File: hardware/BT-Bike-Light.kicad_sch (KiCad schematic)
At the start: 1 part, among them U1 BC805M

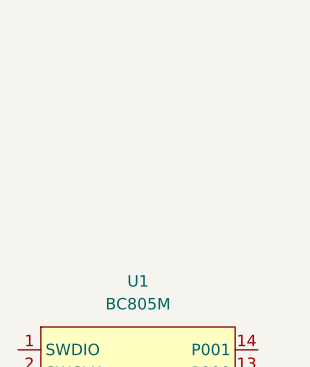
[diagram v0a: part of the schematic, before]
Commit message: Add XPE2 LED
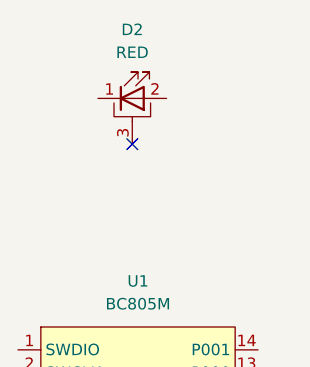
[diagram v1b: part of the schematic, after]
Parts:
- added D2: RED, LED_SMD:LED_Cree-XP, symbol Device:LED_Pad
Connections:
- no-connect marks 0 -> 1
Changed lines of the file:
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@@
 		(comment 1 "Ben Owen")
+	)
+	(no_connect
+		(at 139.7 69.85)
 	)
 	(wire
@@
 		)
 	)
+	(symbol
+		(lib_id "Device:LED_Pad")
+		(at 139.7 64.77 0)
+		(unit 1)
+		(exclude_from_sim no)
+		(in_bom yes)
+		(on_board yes)
+		(dnp no)
+		(fields_autoplaced yes)
+		(property "Reference" "D2"
+			(at 139.7 57.15 0)
+			(effects
+				(font
+					(size 1.27 1.27)
+				)
+			)
+		)
+		(property "Value" "RED"
+			(at 139.7 59.69 0)
+			(effects
+				(font
+					(size 1.27 1.27)
+				)
+			)
+		)
+		(property "Footprint" "LED_SMD:LED_Cree-XP"
+			(at 139.7 64.77 0)
+			(effects
+				(font
+					(size 1.27 1.27)
+				)
+				(hide yes)
+			)
+		)
+		(property "Datasheet" "~"
+			(at 139.7 64.77 0)
+			(effects
+				(font
+					(size 1.27 1.27)
+				)
+				(hide yes)
+			)
+		)
+		(property "Description" "Light emitting diode with pad"
+			(at 139.7 64.77 0)
+			(effects
+				(font
+					(size 1.27 1.27)
+				)
+				(hide yes)
+			)
+		)
+		(pin "2"
+		)
+		(pin "1"
+		)
+		(pin "3"
+		)
+		(instances
+			(project ""
+				(path "/3263b444-391f-435a-aeab-6f7fca8830e2"
+					(reference "D2")
+					(unit 1)
+				)
+			)
+		)
+	)

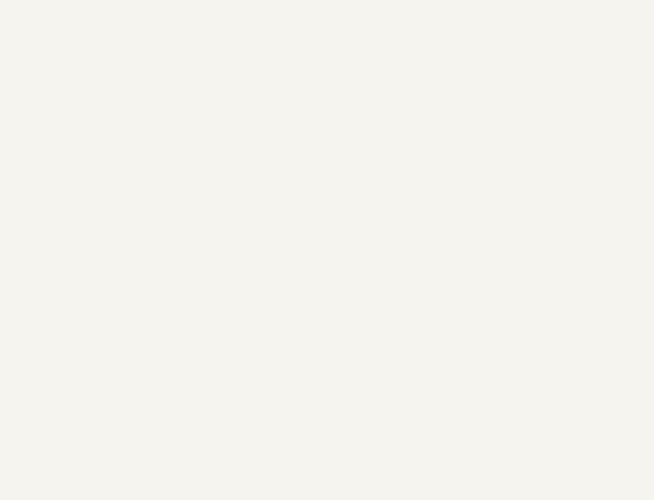
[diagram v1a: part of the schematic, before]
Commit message: Add debug connector
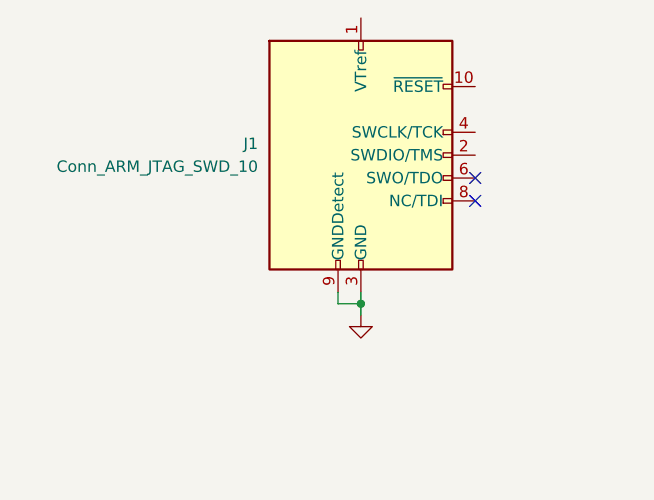
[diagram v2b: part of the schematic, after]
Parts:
- added J1: Conn_ARM_JTAG_SWD_10, Samtech:FTSH-107-01-F-DV-K, symbol Connector:Conn_ARM_JTAG_SWD_10
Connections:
- net GND: now also J1.3 (GND), J1.5 (GND), J1.9 (GNDDetect)
- no-connect marks 1 -> 3
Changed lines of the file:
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@@
 		(comment 1 "Ben Owen")
+	)
+	(junction
+		(at 72.39 63.5)
+		(diameter 0)
+		(color 0 0 0 0)
+	)
+	(no_connect
+		(at 85.09 49.53)
+	)
+	(no_connect
+		(at 85.09 52.07)
 	)
 	(no_connect
@@
 	(wire
 		(pts
+			(xy 72.39 63.5) (xy 72.39 64.77)
+		)
+		(stroke
+			(width 0)
+			(type default)
+		)
+	)
+	(wire
+		(pts
+			(xy 69.85 62.23) (xy 69.85 63.5)
+		)
+		(stroke
+			(width 0)
+			(type default)
+		)
+	)
+	(wire
+		(pts
 			(xy 156.21 110.49) (xy 156.21 107.95)
 		)
@@
 	(wire
 		(pts
+			(xy 72.39 62.23) (xy 72.39 63.5)
+		)
+		(stroke
+			(width 0)
+			(type default)
+		)
+	)
+	(wire
+		(pts
 			(xy 156.21 107.95) (xy 153.67 107.95)
+		)
+		(stroke
+			(width 0)
+			(type default)
+		)
+	)
+	(wire
+		(pts
+			(xy 69.85 63.5) (xy 72.39 63.5)
 		)
 		(stroke
@@
 					(unit 1)
 				)
+			)
+		)
+	)
+	(symbol
+		(lib_id "Connector:Conn_ARM_JTAG_SWD_10")
+		(at 72.39 46.99 0)
+		(unit 1)
+		(exclude_from_sim no)
+		(in_bom yes)
+		(on_board yes)
+		(dnp no)
+		(fields_autoplaced yes)
+		(property "Reference" "J1"
+			(at 60.96 45.7199 0)
+			(effects
+				(font
+					(size 1.27 1.27)
+				)
+				(justify right)
+			)
+		)
+		(property "Value" "Conn_ARM_JTAG_SWD_10"
+			(at 60.96 48.2599 0)
+			(effects
+				(font
+					(size 1.27 1.27)
+				)
+				(justify right)
+			)
+		)
+		(property "Footprint" "Samtech:FTSH-107-01-F-DV-K"
+			(at 72.39 46.99 0)
+			(effects
+				(font
+					(size 1.27 1.27)
+				)
+				(hide yes)
+			)
+		)
+		(property "Datasheet" "http://infocenter.arm.com/help/topic/com.arm.doc.ddi0314h/DDI0314H_coresight_components_trm.pdf"
+			(at 63.5 78.74 90)
+			(effects
+				(font
+					(size 1.27 1.27)
+				)
+				(hide yes)
+			)
+		)
+		(property "Description" "Cortex Debug Connector, standard ARM Cortex-M SWD and JTAG interface"
+			(at 72.39 46.99 0)
+			(effects
+				(font
+					(size 1.27 1.27)
+				)
+				(hide yes)
+			)
+		)
+		(pin "1"
+		)
+		(pin "7"
+		)
+		(pin "10"
+		)
+		(pin "4"
+		)
+		(pin "3"
+		)
+		(pin "8"
+		)
+		(pin "5"
+		)
+		(pin "9"
+		)
+		(pin "6"
+		)
+		(pin "2"
+		)
+		(instances
+			(project ""
+				(path "/3263b444-391f-435a-aeab-6f7fca8830e2"
+					(reference "J1")
+					(unit 1)
+				)
+			)
+		)
+	)
+	(symbol
+		(lib_id "power:GND")
+		(at 72.39 64.77 0)
+		(unit 1)
+		(exclude_from_sim no)
+		(in_bom yes)
+		(on_board yes)
+		(dnp no)
+		(fields_autoplaced yes)
+		(property "Reference" "#PWR02"
+			(at 72.39 71.12 0)
+			(effects
+				(font
+					(size 1.27 1.27)
+				)
+				(hide yes)
+			)
+		)
+		(property "Value" "GND"
+			(at 72.39 69.85 0)
+			(effects
+				(font
+					(size 1.27 1.27)
+				)
+				(hide yes)
+			)
+		)
+		(property "Footprint" ""
+			(at 72.39 64.77 0)
+			(effects
+				(font
+					(size 1.27 1.27)
+				)
+				(hide yes)
+			)
+		)
+		(property "Datasheet" ""
+			(at 72.39 64.77 0)
+			(effects
+				(font
+					(size 1.27 1.27)
+				)
+				(hide yes)
+			)
+		)
+		(property "Description" "Power symbol creates a global label with name \"GND\" , ground"
+			(at 72.39 64.77 0)
+			(effects
+				(font
+					(size 1.27 1.27)
+				)
+				(hide yes)
+			)
+		)
+		(pin "1"
+		)
+		(instances
+			(project "BT-Bike-Light"
+				(path "/3263b444-391f-435a-aeab-6f7fca8830e2"
+					(reference "#PWR02")
+					(unit 1)
+				)

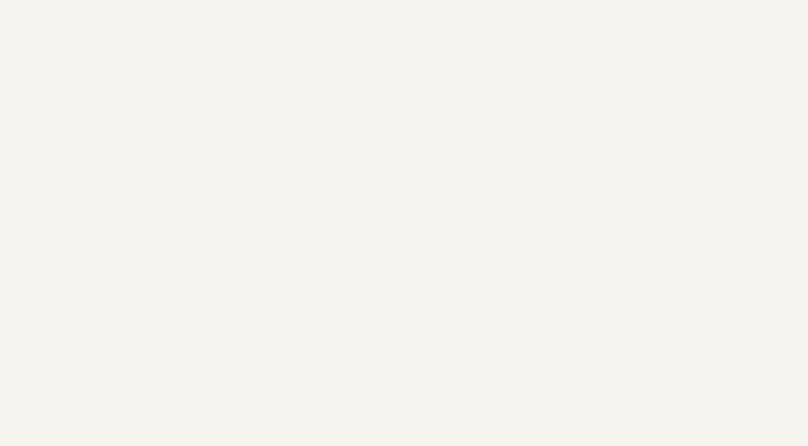
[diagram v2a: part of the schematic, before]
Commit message: Add accelerometer
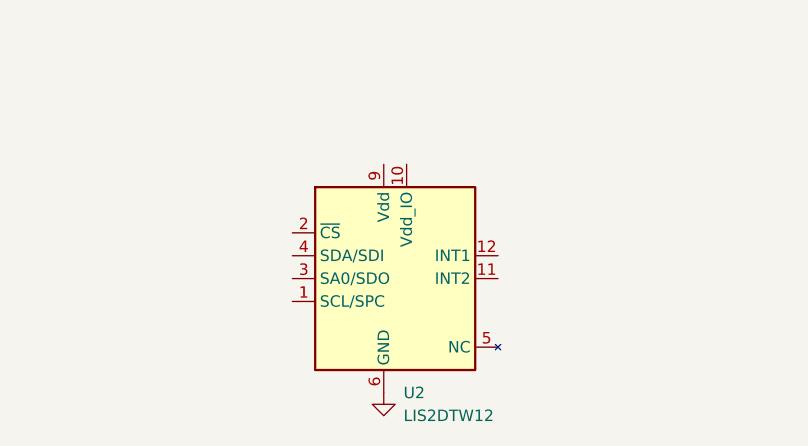
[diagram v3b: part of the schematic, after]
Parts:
- added U2: LIS2DTW12, Package_LGA:LGA-12_2x2mm_P0.5mm, symbol STMicroelectronics:LIS2DTW12
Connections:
- net GND: now also U2.6 (GND), U2.7 (GND), U2.8 (GND)
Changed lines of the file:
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@@
+	)
+	(symbol
+		(lib_id "STMicroelectronics:LIS2DTW12")
+		(at 74.93 100.33 0)
+		(unit 1)
+		(exclude_from_sim no)
+		(in_bom yes)
+		(on_board yes)
+		(dnp no)
+		(fields_autoplaced yes)
+		(property "Reference" "U2"
+			(at 77.1241 113.03 0)
+			(effects
+				(font
+					(size 1.27 1.27)
+				)
+				(justify left)
+			)
+		)
+		(property "Value" "LIS2DTW12"
+			(at 77.1241 115.57 0)
+			(effects
+				(font
+					(size 1.27 1.27)
+				)
+				(justify left)
+			)
+		)
+		(property "Footprint" "Package_LGA:LGA-12_2x2mm_P0.5mm"
+			(at 78.74 86.36 0)
+			(effects
+				(font
+					(size 1.27 1.27)
+				)
+				(justify left)
+				(hide yes)
+			)
+		)
+		(property "Datasheet" "https://www.st.com/resource/en/datasheet/lis2dtw12.pdf"
+			(at 66.04 100.33 0)
+			(effects
+				(font
+					(size 1.27 1.27)
+				)
+				(hide yes)
+			)
+		)
+		(property "Description" "MEMS digital output dual motion and temperature sensor"
+			(at 74.93 100.33 0)
+			(effects
+				(font
+					(size 1.27 1.27)
+				)
+				(hide yes)
+			)
+		)
+		(pin "2"
+		)
+		(pin "3"
+		)
+		(pin "4"
+		)
+		(pin "12"
+		)
+		(pin "11"
+		)
+		(pin "10"
+		)
+		(pin "8"
+		)
+		(pin "9"
+		)
+		(pin "6"
+		)
+		(pin "5"
+		)
+		(pin "7"
+		)
+		(pin "1"
+		)
+		(instances
+			(project ""
+				(path "/3263b444-391f-435a-aeab-6f7fca8830e2"
+					(reference "U2")
+					(unit 1)
+				)
+			)
+		)
 	)
 	(symbol
@@
 					(unit 1)
 				)
+			)
+		)
+	)
+	(symbol
+		(lib_id "power:GND")
+		(at 74.93 113.03 0)
+		(unit 1)
+		(exclude_from_sim no)
+		(in_bom yes)
+		(on_board yes)
+		(dnp no)
+		(fields_autoplaced yes)
+		(property "Reference" "#PWR03"
+			(at 74.93 119.38 0)
+			(effects
+				(font
+					(size 1.27 1.27)
+				)
+				(hide yes)
+			)
+		)
+		(property "Value" "GND"
+			(at 74.93 118.11 0)
+			(effects
+				(font
+					(size 1.27 1.27)
+				)
+				(hide yes)
+			)
+		)
+		(property "Footprint" ""
+			(at 74.93 113.03 0)
+			(effects
+				(font
+					(size 1.27 1.27)
+				)
+				(hide yes)
+			)
+		)
+		(property "Datasheet" ""
+			(at 74.93 113.03 0)
+			(effects
+				(font
+					(size 1.27 1.27)
+				)
+				(hide yes)
+			)
+		)
+		(property "Description" "Power symbol creates a global label with name \"GND\" , ground"
+			(at 74.93 113.03 0)
+			(effects
+				(font
+					(size 1.27 1.27)
+				)
+				(hide yes)
+			)
+		)
+		(pin "1"
+		)
+		(instances
+			(project "BT-Bike-Light"
+				(path "/3263b444-391f-435a-aeab-6f7fca8830e2"
+					(reference "#PWR03")
+					(unit 1)
+				)

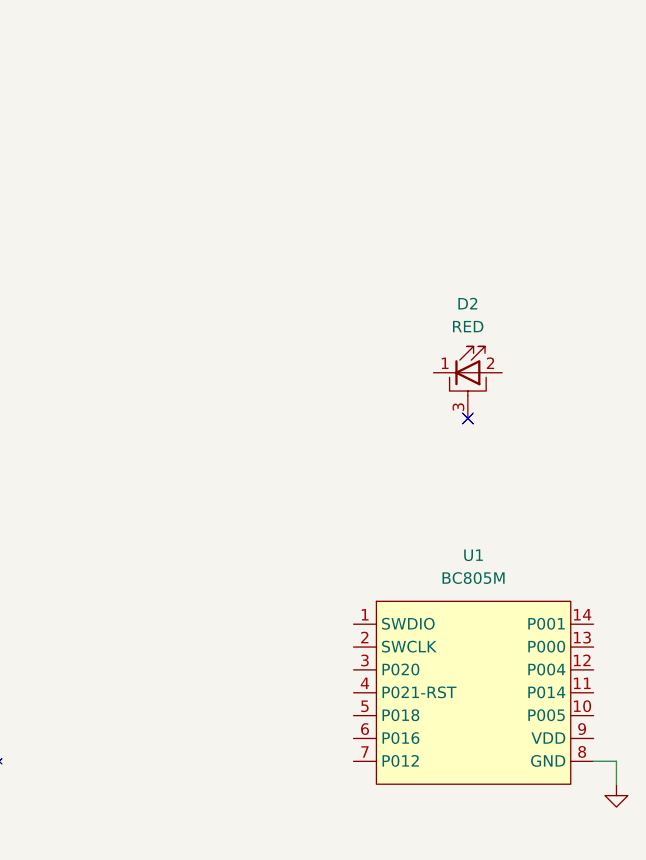
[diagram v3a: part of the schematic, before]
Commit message: Add LED driver
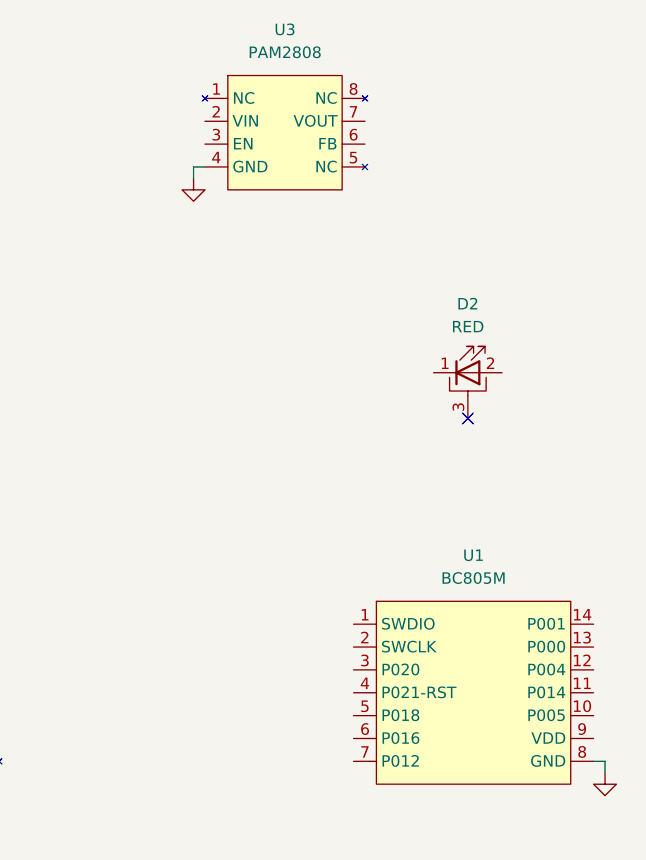
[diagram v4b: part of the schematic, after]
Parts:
- added U3: PAM2808, Package_SO:Diodes_SO-8EP, symbol Diodes-Incorporated:PAM2808
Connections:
- net GND: now also U3.4 (GND)
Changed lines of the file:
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@@
 	(wire
 		(pts
-			(xy 156.21 110.49) (xy 156.21 107.95)
+			(xy 154.94 109.22) (xy 154.94 107.95)
 		)
 		(stroke
@@
 	(wire
 		(pts
-			(xy 156.21 107.95) (xy 153.67 107.95)
+			(xy 154.94 107.95) (xy 153.67 107.95)
 		)
 		(stroke
@@
 	(wire
 		(pts
-			(xy 69.85 63.5) (xy 72.39 63.5)
+			(xy 110.49 41.91) (xy 109.22 41.91)
 		)
 		(stroke
@@
 		)
 	)
+	(wire
+		(pts
+			(xy 109.22 41.91) (xy 109.22 43.18)
+		)
+		(stroke
+			(width 0)
+			(type default)
+		)
+	)
+	(wire
+		(pts
+			(xy 69.85 63.5) (xy 72.39 63.5)
+		)
+		(stroke
+			(width 0)
+			(type default)
+		)
+	)
+	(symbol
+		(lib_id "power:GND")
+		(at 109.22 43.18 0)
+		(unit 1)
+		(exclude_from_sim no)
+		(in_bom yes)
+		(on_board yes)
+		(dnp no)
+		(fields_autoplaced yes)
+		(property "Reference" "#PWR04"
+			(at 109.22 49.53 0)
+			(effects
+				(font
+					(size 1.27 1.27)
+				)
+				(hide yes)
+			)
+		)
+		(property "Value" "GND"
+			(at 109.22 48.26 0)
+			(effects
+				(font
+					(size 1.27 1.27)
+				)
+				(hide yes)
+			)
+		)
+		(property "Footprint" ""
+			(at 109.22 43.18 0)
+			(effects
+				(font
+					(size 1.27 1.27)
+				)
+				(hide yes)
+			)
+		)
+		(property "Datasheet" ""
+			(at 109.22 43.18 0)
+			(effects
+				(font
+					(size 1.27 1.27)
+				)
+				(hide yes)
+			)
+		)
+		(property "Description" "Power symbol creates a global label with name \"GND\" , ground"
+			(at 109.22 43.18 0)
+			(effects
+				(font
+					(size 1.27 1.27)
+				)
+				(hide yes)
+			)
+		)
+		(pin "1"
+		)
+		(instances
+			(project "BT-Bike-Light"
+				(path "/3263b444-391f-435a-aeab-6f7fca8830e2"
+					(reference "#PWR04")
+					(unit 1)
+				)
+			)
+		)
+	)
 	(symbol
 		(lib_id "STMicroelectronics:LIS2DTW12")
@@
 	(symbol
 		(lib_id "power:GND")
-		(at 156.21 110.49 0)
+		(at 154.94 109.22 0)
 		(unit 1)
 		(exclude_from_sim no)
@@
 		(fields_autoplaced yes)
 		(property "Reference" "#PWR01"
-			(at 156.21 116.84 0)
+			(at 154.94 115.57 0)
 			(effects
 				(font
@@
 		)
 		(property "Value" "GND"
-			(at 156.21 115.57 0)
+			(at 154.94 114.3 0)
 			(effects
 				(font
@@
 		)
 		(property "Footprint" ""
-			(at 156.21 110.49 0)
+			(at 154.94 109.22 0)
 			(effects
 				(font
@@
 		)
 		(property "Datasheet" ""
-			(at 156.21 110.49 0)
+			(at 154.94 109.22 0)
 			(effects
 				(font
@@
 		)
 		(property "Description" "Power symbol creates a global label with name \"GND\" , ground"
-			(at 156.21 110.49 0)
+			(at 154.94 109.22 0)
 			(effects
 				(font
@@
 					(unit 1)
 				)
+			)
+		)
+	)
+	(symbol
+		(lib_id "Diodes-Incorporated:PAM2808")
+		(at 119.38 38.1 0)
+		(unit 1)
+		(exclude_from_sim no)
+		(in_bom yes)
+		(on_board yes)
+		(dnp no)
+		(fields_autoplaced yes)
+		(property "Reference" "U3"
+			(at 119.38 26.67 0)
+			(effects
+				(font
+					(size 1.27 1.27)
+				)
+			)
+		)
+		(property "Value" "PAM2808"
+			(at 119.38 29.21 0)
+			(effects
+				(font
+					(size 1.27 1.27)
+				)
+			)
+		)
+		(property "Footprint" "Package_SO:Diodes_SO-8EP"
+			(at 119.38 38.1 0)
+			(effects
+				(font
+					(size 1.27 1.27)
+				)
+				(hide yes)
+			)
+		)
+		(property "Datasheet" "https://www.diodes.com/assets/Datasheets/PAM2808.pdf"
+			(at 119.38 38.1 0)
+			(effects
+				(font
+					(size 1.27 1.27)
+				)
+				(hide yes)
+			)
+		)
+		(property "Description" "5W high power HBLED driver with 1.5A constant current"
+			(at 119.38 38.1 0)
+			(effects
+				(font
+					(size 1.27 1.27)
+				)
+				(hide yes)
+			)
+		)
+		(pin "6"
+		)
+		(pin "4"
+		)
+		(pin "3"
+		)
+		(pin "8"
+		)
+		(pin "7"
+		)
+		(pin "1"
+		)
+		(pin "5"
+		)
+		(pin "2"
+		)
+		(instances
+			(project ""
+				(path "/3263b444-391f-435a-aeab-6f7fca8830e2"
+					(reference "U3")
+					(unit 1)
+				)

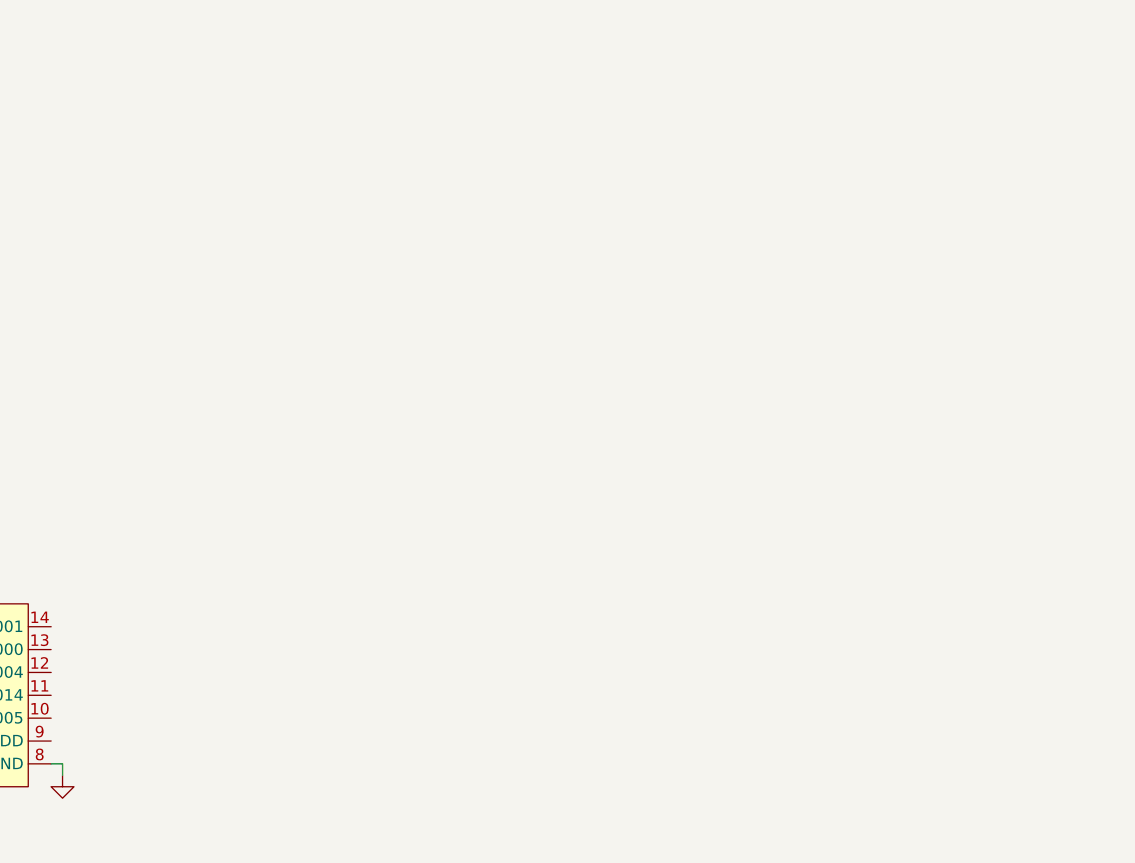
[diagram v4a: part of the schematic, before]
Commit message: Add USB/UART bridge
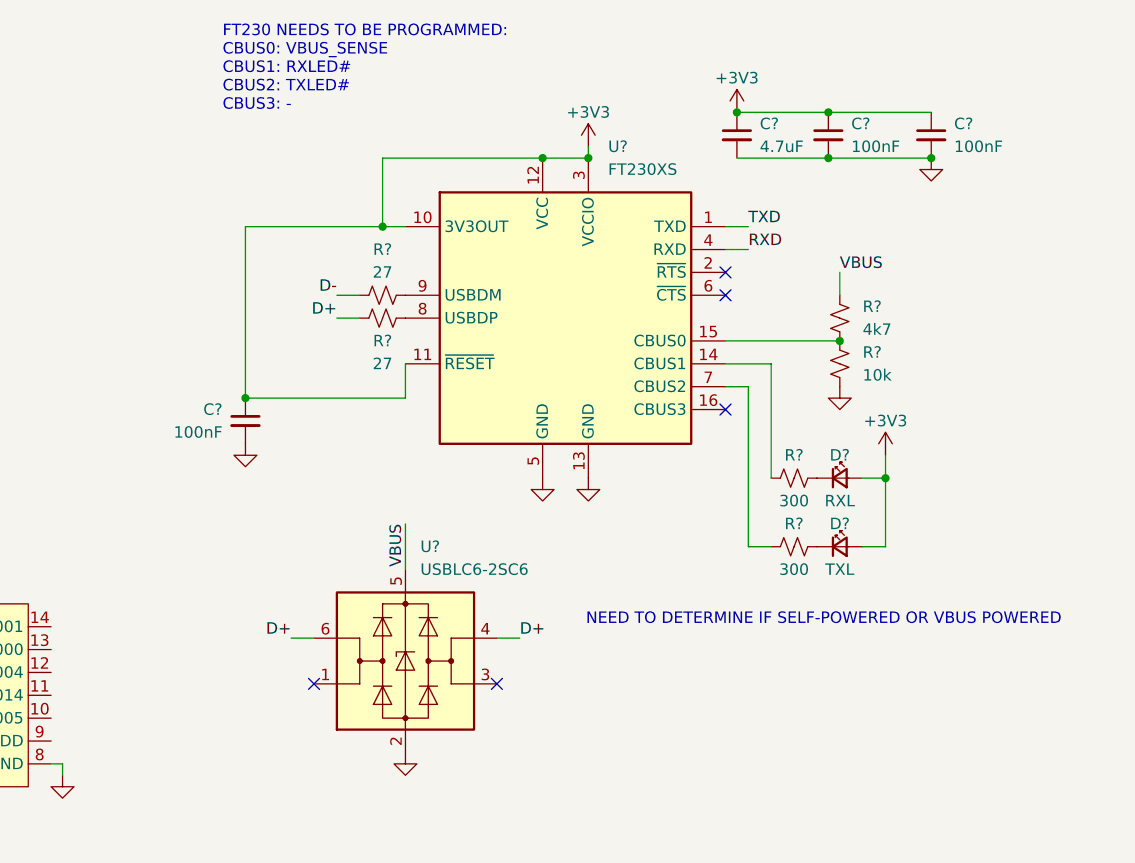
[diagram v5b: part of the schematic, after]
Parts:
- added C?: 4.7uF, Capacitor_SMD:C_0805_2012Metric_Pad1.18x1.45mm_HandSolder, symbol Device:C_Small
- added C? (x3): 100nF, Capacitor_SMD:C_0805_2012Metric_Pad1.18x1.45mm_HandSolder, symbol Device:C_Small
- added D?: RXL, LED_SMD:LED_0805_2012Metric_Pad1.15x1.40mm_HandSolder, symbol Device:LED_Small
- added D?: TXL, LED_SMD:LED_0805_2012Metric_Pad1.15x1.40mm_HandSolder, symbol Device:LED_Small
- added R? (x2): 27, Resistor_SMD:R_0805_2012Metric_Pad1.20x1.40mm_HandSolder, symbol Device:R_Small_US
- added R?: 4k7, Resistor_SMD:R_0805_2012Metric_Pad1.20x1.40mm_HandSolder, symbol Device:R_Small_US
- added R? (x2): 300, Resistor_SMD:R_0805_2012Metric_Pad1.20x1.40mm_HandSolder, symbol Device:R_Small_US
- added R?: 10k, Resistor_SMD:R_0805_2012Metric_Pad1.20x1.40mm_HandSolder, symbol Device:R_Small_US
- added U?: FT230XS, Package_SO:SSOP-16_3.9x4.9mm_P0.635mm, symbol Interface_USB:FT230XS
- added U?: USBLC6-2SC6, Package_TO_SOT_SMD:SOT-23-6, symbol Power_Protection:USBLC6-2SC6
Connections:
- net GND: now also C?.2, C?.2, C?.2, C?.2, R?.2, U?.13 (GND), U?.2 (GND), U?.5 (GND)
- new net: R?.2, U?.9 (USBDM)
- new net: R?.1, R?.2, U?.15 (CBUS0)
- new net: D?.1 (K), R?.2 (x2)
- new net: R?.1, U?.14 (CBUS1)
- new net: R?.1, U?.7 (CBUS2)
- new net: R?.2, U?.8 (USBDP)
- new net +3V3: C?.1, C?.1, C?.1, C?.1, D?.2 (A), D?.2 (A), U?.10 (3V3OUT), U?.11 (~{RESET}), U?.12 (VCC), U?.3 (VCCIO)
- new net D+: R?.1, U?.4 (I/O2), U?.6 (I/O1)
- new net D-: R?.1
- new net RXD: U?.4 (RXD)
- new net TXD: U?.1 (TXD)
- new net VBUS: R?.1, U?.5 (VBUS)
- no-connect marks 3 -> 8
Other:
- note added: "FT230 NEEDS TO BE PROGRAMMED: CBUS0: VBUS_SENSE CBUS1: RXLED# CBUS2: TXLED# CBUS3: -"
- note added: "NEED TO DETERMINE IF SELF-POWERED OR VBUS POWERED"
